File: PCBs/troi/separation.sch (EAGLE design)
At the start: 3 parts

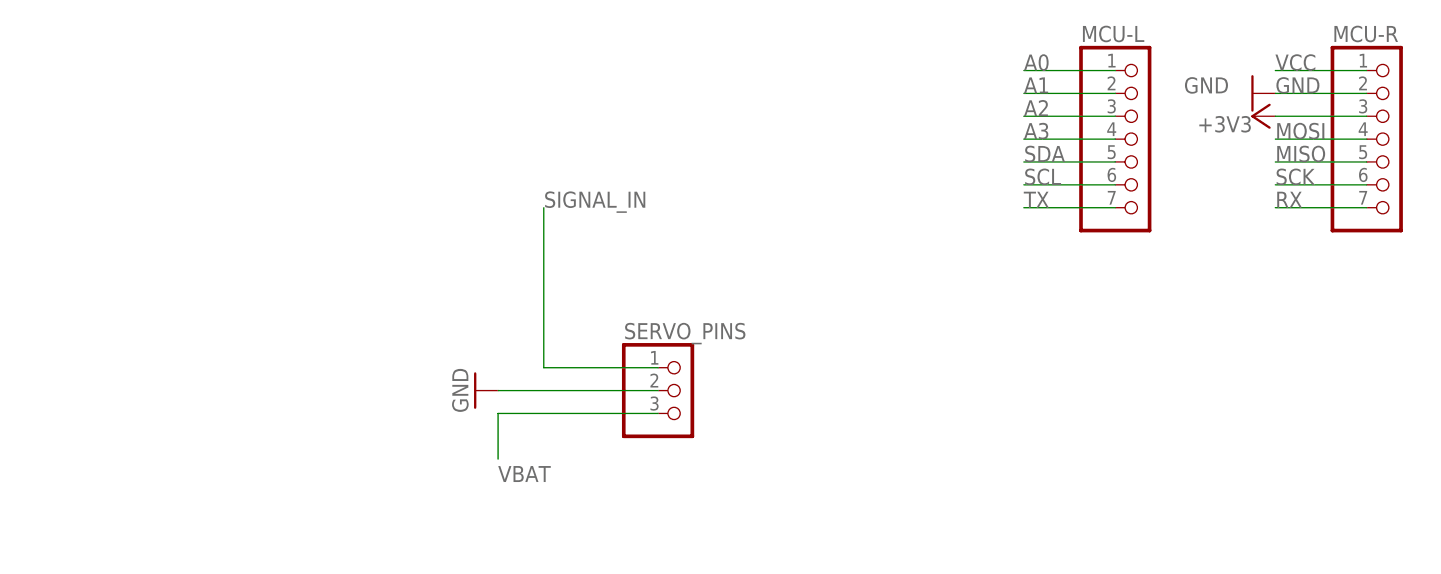
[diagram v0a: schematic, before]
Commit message: Added MOSIFET
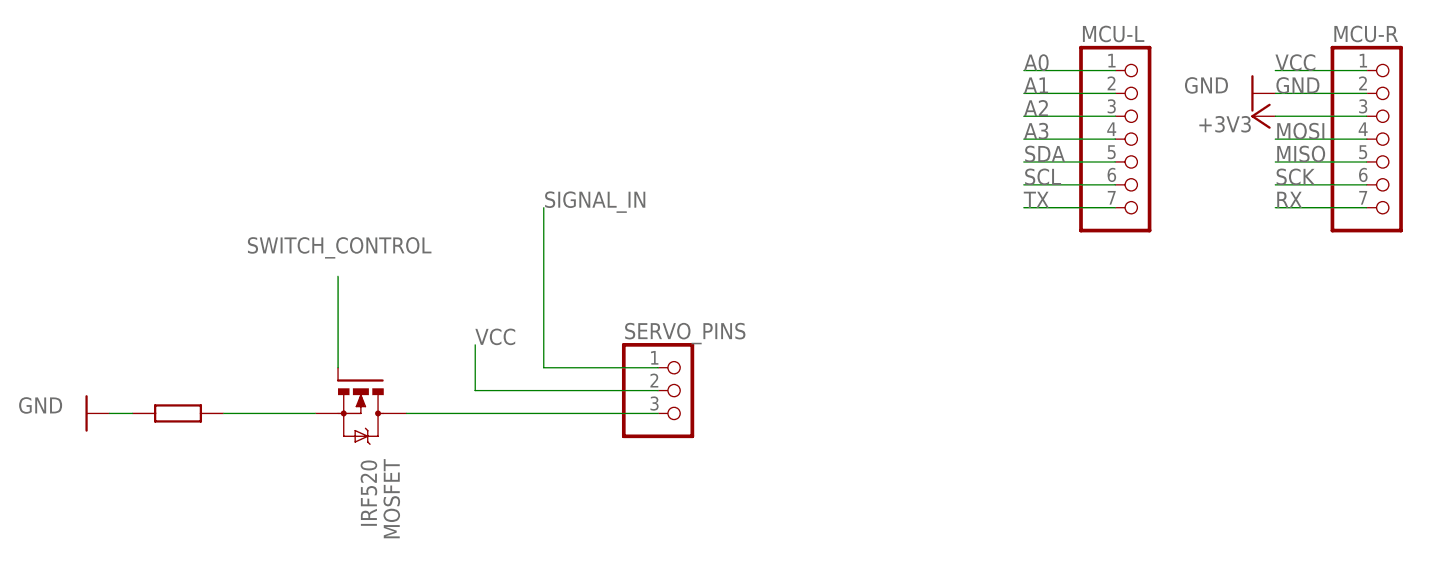
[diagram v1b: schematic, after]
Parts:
- added MOSFET: IRF520, transistor-power:IRF520
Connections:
- removed net VBAT: SERVO_PINS.3
- new net N$1: MOSFET.D, SERVO_PINS.3
- new net N$2: MOSFET.S
- new net SWITCH_CONTROL: MOSFET.G
- net GND: no longer SERVO_PINS.2
- net VCC: now also SERVO_PINS.2
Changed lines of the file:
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@@
 <grid distance="0.1" unitdist="inch" unit="inch" style="lines" multiple="1" display="no" altdistance="0.01" altunitdist="inch" altunit="inch"/>
 <layers>
-<layer number="1" name="Top" color="4" fill="1" visible="no" active="no"/>
-<layer number="16" name="Bottom" color="1" fill="1" visible="no" active="no"/>
-<layer number="17" name="Pads" color="2" fill="1" visible="no" active="no"/>
-<layer number="18" name="Vias" color="2" fill="1" visible="no" active="no"/>
-<layer number="19" name="Unrouted" color="6" fill="1" visible="no" active="no"/>
-<layer number="20" name="Dimension" color="15" fill="1" visible="no" active="no"/>
-<layer number="21" name="tPlace" color="7" fill="1" visible="no" active="no"/>
-<layer number="22" name="bPlace" color="7" fill="1" visible="no" active="no"/>
-<layer number="23" name="tOrigins" color="15" fill="1" visible="no" active="no"/>
-<layer number="24" name="bOrigins" color="15" fill="1" visible="no" active="no"/>
-<layer number="25" name="tNames" color="7" fill="1" visible="no" active="no"/>
-<layer number="26" name="bNames" color="7" fill="1" visible="no" active="no"/>
-<layer number="27" name="tValues" color="7" fill="1" visible="no" active="no"/>
-<layer number="28" name="bValues" color="7" fill="1" visible="no" active="no"/>
+<layer number="1" name="Top" color="4" fill="1" visible="yes" active="no"/>
+<layer number="16" name="Bottom" color="1" fill="1" visible="yes" active="no"/>
+<layer number="17" name="Pads" color="2" fill="1" visible="yes" active="no"/>
+<layer number="18" name="Vias" color="2" fill="1" visible="yes" active="no"/>
+<layer number="19" name="Unrouted" color="6" fill="1" visible="yes" active="no"/>
+<layer number="20" name="Dimension" color="15" fill="1" visible="yes" active="no"/>
+<layer number="21" name="tPlace" color="7" fill="1" visible="yes" active="no"/>
+<layer number="22" name="bPlace" color="7" fill="1" visible="yes" active="no"/>
+<layer number="23" name="tOrigins" color="15" fill="1" visible="yes" active="no"/>
+<layer number="24" name="bOrigins" color="15" fill="1" visible="yes" active="no"/>
+<layer number="25" name="tNames" color="7" fill="1" visible="yes" active="no"/>
+<layer number="26" name="bNames" color="7" fill="1" visible="yes" active="no"/>
+<layer number="27" name="tValues" color="7" fill="1" visible="yes" active="no"/>
+<layer number="28" name="bValues" color="7" fill="1" visible="yes" active="no"/>
 <layer number="29" name="tStop" color="7" fill="3" visible="no" active="no"/>
 <layer number="30" name="bStop" color="7" fill="6" visible="no" active="no"/>
@@
 <layer number="35" name="tGlue" color="7" fill="4" visible="no" active="no"/>
 <layer number="36" name="bGlue" color="7" fill="5" visible="no" active="no"/>
-<layer number="37" name="tTest" color="7" fill="1" visible="no" active="no"/>
-<layer number="38" name="bTest" color="7" fill="1" visible="no" active="no"/>
+<layer number="37" name="tTest" color="7" fill="1" visible="yes" active="no"/>
+<layer number="38" name="bTest" color="7" fill="1" visible="yes" active="no"/>
 <layer number="39" name="tKeepout" color="4" fill="11" visible="no" active="no"/>
 <layer number="40" name="bKeepout" color="1" fill="11" visible="no" active="no"/>
@@
 <layer number="44" name="Drills" color="7" fill="1" visible="no" active="no"/>
 <layer number="45" name="Holes" color="7" fill="1" visible="no" active="no"/>
-<layer number="46" name="Milling" color="3" fill="1" visible="no" active="no"/>
-<layer number="47" name="Measures" color="7" fill="1" visible="no" active="no"/>
-<layer number="48" name="Document" color="7" fill="1" visible="no" active="no"/>
-<layer number="49" name="Reference" color="7" fill="1" visible="no" active="no"/>
-<layer number="51" name="tDocu" color="7" fill="1" visible="no" active="no"/>
-<layer number="52" name="bDocu" color="7" fill="1" visible="no" active="no"/>
+<layer number="46" name="Milling" color="3" fill="1" visible="yes" active="no"/>
+<layer number="47" name="Measures" color="7" fill="1" visible="yes" active="no"/>
+<layer number="48" name="Document" color="7" fill="1" visible="yes" active="no"/>
+<layer number="49" name="Reference" color="7" fill="1" visible="yes" active="no"/>
+<layer number="51" name="tDocu" color="7" fill="1" visible="yes" active="no"/>
+<layer number="52" name="bDocu" color="7" fill="1" visible="yes" active="no"/>
 <layer number="88" name="SimResults" color="9" fill="1" visible="yes" active="yes"/>
 <layer number="89" name="SimProbes" color="9" fill="1" visible="yes" active="yes"/>
@@
 <part name="GND1" library="supply1" library_urn="urn:adsk.eagle:library:371" deviceset="GND" device=""/>
 <part name="SERVO_PINS" library="pinhead" library_urn="urn:adsk.eagle:library:325" deviceset="PINHD-1X3" device="" package3d_urn="urn:adsk.eagle:package:22458/2"/>
+<part name="MOSFET" library="transistor-power" library_urn="urn:adsk.eagle:library:400" deviceset="IRF520" device="" package3d_urn="urn:adsk.eagle:package:29484/3"/>
+<part name="R1" library="docu-dummy" library_urn="urn:adsk.eagle:library:215" deviceset="R" device=""/>
 <part name="GND2" library="supply1" library_urn="urn:adsk.eagle:library:371" deviceset="GND" device=""/>
 </parts>
@@
 <attribute name="VALUE" x="24.13" y="45.72" size="1.778" layer="96"/>
 </instance>
-<instance part="GND2" gate="1" x="7.62" y="53.34" smashed="yes" rot="R270">
-<attribute name="VALUE" x="5.08" y="55.88" size="1.778" layer="96" rot="R270"/>
+<instance part="MOSFET" gate="G$1" x="-5.08" y="53.34" smashed="yes" rot="R270">
+<attribute name="NAME" x="-2.54" y="45.72" size="1.778" layer="95" rot="R270"/>
+<attribute name="VALUE" x="-5.08" y="45.72" size="1.778" layer="96" rot="R270"/>
+</instance>
+<instance part="R1" gate="G$1" x="-25.4" y="50.8" smashed="yes"/>
+<instance part="GND2" gate="1" x="-35.56" y="50.8" smashed="yes" rot="R270">
+<attribute name="VALUE" x="-43.18" y="50.8" size="1.778" layer="96"/>
 </instance>
 </instances>
@@
 <label x="96.52" y="88.9" size="1.778" layer="95"/>
 </segment>
+<segment>
+<pinref part="SERVO_PINS" gate="A" pin="2"/>
+<wire x1="27.94" y1="53.34" x2="7.62" y2="53.34" width="0.1524" layer="91"/>
+<wire x1="7.62" y1="53.34" x2="7.62" y2="58.42" width="0.1524" layer="91"/>
+<label x="7.62" y="58.42" size="1.778" layer="95"/>
+</segment>
 </net>
 <net name="GND" class="0">
@@
 </segment>
 <segment>
-<pinref part="SERVO_PINS" gate="A" pin="2"/>
-<wire x1="27.94" y1="53.34" x2="10.16" y2="53.34" width="0.1524" layer="91"/>
 <pinref part="GND2" gate="1" pin="GND"/>
+<wire x1="-33.02" y1="50.8" x2="-30.48" y2="50.8" width="0.1524" layer="91"/>
 </segment>
 </net>
@@
 </segment>
 </net>
-<net name="VBAT" class="0">
-<segment>
+<net name="N$2" class="0">
+<segment>
+<pinref part="MOSFET" gate="G$1" pin="S"/>
+<wire x1="-10.16" y1="50.8" x2="-20.32" y2="50.8" width="0.1524" layer="91"/>
+</segment>
+</net>
+<net name="SWITCH_CONTROL" class="0">
+<segment>
+<pinref part="MOSFET" gate="G$1" pin="G"/>
+<wire x1="-7.62" y1="55.88" x2="-7.62" y2="66.04" width="0.1524" layer="91"/>
+<label x="-17.78" y="68.58" size="1.778" layer="95"/>
+</segment>
+</net>
+<net name="N$1" class="0">
+<segment>
+<pinref part="MOSFET" gate="G$1" pin="D"/>
 <pinref part="SERVO_PINS" gate="A" pin="3"/>
-<wire x1="27.94" y1="50.8" x2="10.16" y2="50.8" width="0.1524" layer="91"/>
-<wire x1="10.16" y1="50.8" x2="10.16" y2="45.72" width="0.1524" layer="91"/>
-<label x="10.16" y="43.18" size="1.778" layer="95"/>
-</segment>
-</net>
+<wire x1="0" y1="50.8" x2="27.94" y2="50.8" width="0.1524" layer="91"/>
+</segment>
+</net>
